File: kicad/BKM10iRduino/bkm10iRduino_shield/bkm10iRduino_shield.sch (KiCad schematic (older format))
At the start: 6 parts, among them J1 RJ45, SW1 SW_SPST, U1 TSOP343xx, U2 MAX485E

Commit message: updated pcb design
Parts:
- removed Brd1: SSD1306, SSD1306:128x64OLED, symbol SSD1306-128x64_OLED:SSD1306
- removed J1: RJ45, Connector_RJ:RJ45_Amphenol_54602-x08_Horizontal, symbol Connector:RJ45
- added C1: C_Small, Capacitor_SMD:CP_Elec_3x5.3, symbol Device:C_Small
- added D3, D4: D_Small_ALT, Diode_SMD:D_1206_3216Metric_Pad1.42x1.75mm_HandSolder, symbol Device:D_Small_ALT
- added D5: SH1106, Connector_PinHeader_2.54mm:PinHeader_1x07_P2.54mm_Vertical, symbol bkm10:SH1106
- added J1: DB9_Male, Connector_Dsub:DSUB-9_Male_Horizontal_P2.77x2.84mm_EdgePinOffset4.94mm_Housed_MountingHolesOffset7.48mm, symbol Connector:DB9_Male
- added R1: R, Resistor_SMD:R_1206_3216Metric_Pad1.30x1.75mm_HandSolder, symbol Device:R
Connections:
- net GND: now also C1.2, D5.7 (GND), J1.1, J1.4, J1.6, J1.9
- net VCC: now also C1.1, D5.6 (VCC), J1.5
- net RES: now reaches A1.11 (D8)
- net RES: now also D5.3 (RES)
- net CS: now reaches A1.12 (D9)
- net CS: now also D5.1 (CS)
- net DC: now reaches A1.13 (D10)
- net DC: now also D5.2 (DC)
- net MOSI: now reaches A1.14 (MOSI)
- net MOSI: now also D5.4 (MOSI)
- net SCK: now reaches A1.16 (SCK)
- net SCK: now also D5.5 (CLK)
- net RS485_RX: now reaches A1.2 (RX1)
- net RS485_RX: now also U2.1 (RO)
- net RS485_RX_ENABLE: now reaches A1.6 (D3)
- net RS485_RX_ENABLE: now also U2.2 (~RE)
- net AB+: now reaches U2.6 (A)
- net AB+: now also D3.1 (K), J1.2, R1.1
- net AB-: now reaches U2.7 (B)
- net AB-: now also D4.1 (K), J1.7, R1.2
- net ~LEARN_BUTTON_IN renamed LEARN_BUTTON_IN
- new net YZ+: D3.2 (A), J1.3
- new net YZ-: D4.2 (A), J1.8
- no-connect marks 25 -> 16

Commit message: pcb redesign
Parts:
- removed D3, D4: D_Small_ALT, Diode_SMD:D_1206_3216Metric_Pad1.42x1.75mm_HandSolder, symbol Device:D_Small_ALT
- removed U2: MAX485E, bkm10rduino:TLL_RS485, symbol Interface_UART:MAX485E
- added C2, C3, C4: C_Small, Capacitor_SMD:C_1812_4532Metric_Pad1.57x3.40mm_HandSolder, symbol Device:C_Small
- added IC1: MAX22508EASA+, SOP50P490X110-10N, symbol SamacSys_Parts:MAX22508EASA+
- C1: footprint Capacitor_SMD:CP_Elec_3x5.3 -> Capacitor_SMD:C_1812_4532Metric_Pad1.57x3.40mm_HandSolder
- J1: footprint Connector_Dsub:DSUB-9_Male_Horizontal_P2.77x2.84mm_EdgePinOffset4.94mm_Housed_MountingHolesOffset7.48mm -> Connector_Dsub:DSUB-9_Male_Vertical_P2.77x2.84mm_MountingHoles
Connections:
- net AB+: now also J1.7, IC1.8 (A); no longer J1.2, R1.1
- net AB-: now also J1.2, IC1.9 (B); no longer J1.7, R1.2
- net GND: now also C2.2, C3.1, C4.1, IC1.5 (GND)
- net RS485_RX: now also IC1.1 (RO)
- net RS485_RX_ENABLE: now also A1.5 (D2), IC1.2 (RE); no longer A1.6 (D3)
- net RS485_TX: now also IC1.4 (DI)
- net RS485_TX_ENABLE: now also A1.6 (D3), IC1.3 (DE); no longer A1.5 (D2)
- net VCC: now also C2.1, C3.2, C4.2, IC1.10 (VCC)
- net YZ+: now also R1.1, IC1.6 (Y)
- net YZ-: now also R1.2, IC1.7 (Z)
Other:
- moved on the sheet: A1, C1, D5, R1, SW1, U1

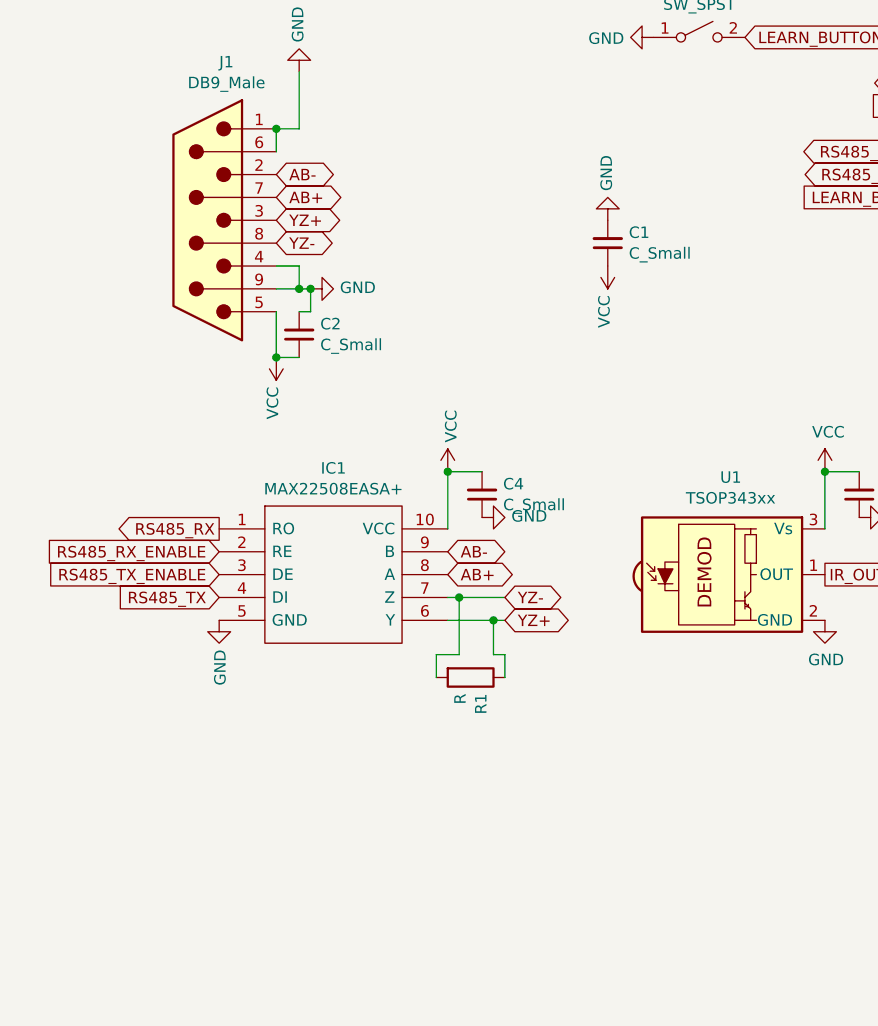
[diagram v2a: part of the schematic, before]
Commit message: many fixes to pcb layout, use full duplex RS485
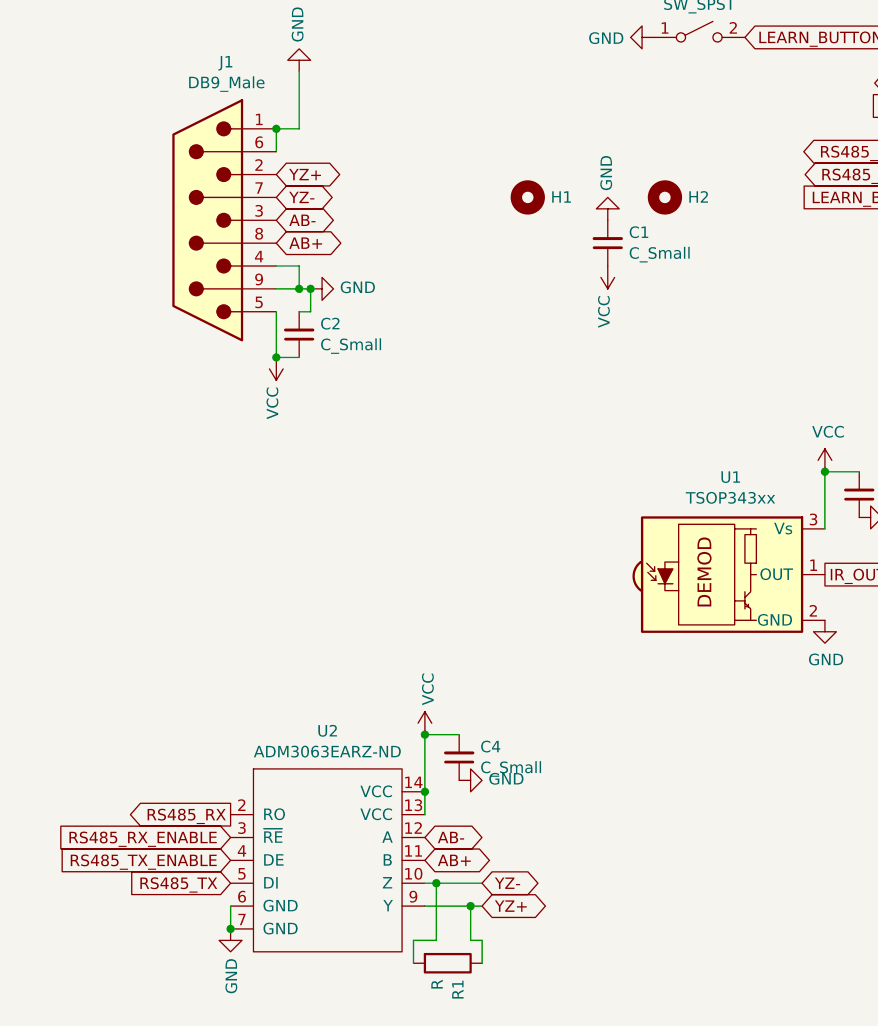
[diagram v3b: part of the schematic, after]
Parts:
- removed IC1: MAX22508EASA+, SOP50P490X110-10N, symbol SamacSys_Parts:MAX22508EASA+
- added H1, H2: MountingHole, MountingHole:MountingHole_3.2mm_M3, symbol Mechanical:MountingHole
- added U2: ADM3063EARZ-ND, Package_SO:SOIC-14_3.9x8.7mm_P1.27mm, symbol bkm10:ADM3063EARZ-ND
- C1, C2, C3, C4: footprint Capacitor_SMD:C_1812_4532Metric_Pad1.57x3.40mm_HandSolder -> Capacitor_SMD:C_1206_3216Metric_Pad1.33x1.80mm_HandSolder
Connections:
- net AB+: now also J1.8, U2.11 (B); no longer J1.7
- net AB-: now also J1.3, U2.12 (A); no longer J1.2
- net GND: now also U2.6 (GND), U2.7 (GND)
- net RS485_RX: now also U2.2 (RO)
- net RS485_RX_ENABLE: now also U2.3 (~RE)
- net RS485_TX: now also U2.5 (DI)
- net RS485_TX_ENABLE: now also U2.4 (DE)
- net VCC: now also U2.13 (VCC), U2.14 (VCC)
- net YZ+: now also J1.2, U2.9 (Y); no longer J1.3
- net YZ-: now also J1.7, U2.10 (Z); no longer J1.8
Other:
- moved on the sheet: C4, R1
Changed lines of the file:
@@
 Text GLabel 6850 2550 0    50   Input ~ 0
 IR_OUT
-Text GLabel 3550 4000 0    50   Input ~ 0
+Text GLabel 3600 5250 0    50   Input ~ 0
 RS485_TX
 Text GLabel 6850 1750 0    50   Output ~ 0
 RS485_TX
-Text GLabel 3550 3900 0    50   Input ~ 0
+Text GLabel 3600 5150 0    50   Input ~ 0
 RS485_TX_ENABLE
 Text GLabel 6850 2150 0    50   Output ~ 0
@@
 Text GLabel 6850 2250 0    50   Input ~ 0
 LEARN_BUTTON_IN
-Text GLabel 3550 3800 0    50   Input ~ 0
+Text GLabel 3600 5050 0    50   Input ~ 0
 RS485_RX_ENABLE
 Text GLabel 6850 2050 0    50   Output ~ 0
 RS485_RX_ENABLE
-Text GLabel 3550 3700 0    50   Output ~ 0
+Text GLabel 3600 4950 0    50   Output ~ 0
 RS485_RX
 Text GLabel 6850 1850 0    50   Input ~ 0
@@
 F 0 "C1" H 5158 2404 50  0000 R CNN
 F 1 "C_Small" H 5158 2495 50  0000 R CNN
-F 2 "Capacitor_SMD:C_1812_4532Metric_Pad1.57x3.40mm_HandSolder" H 5250 2450 50  0001 C CNN
+F 2 "Capacitor_SMD:C_1206_3216Metric_Pad1.33x1.80mm_HandSolder" H 5250 2450 50  0001 C CNN
 F 3 "~" H 5250 2450 50  0001 C CNN
 	1    5250 2450
@@
 L Device:R R1
 U 1 1 618A676D
-P 4650 4350
-F 0 "R1" H 4720 4396 50  0000 L CNN
-F 1 "R" H 4720 4305 50  0000 L CNN
-F 2 "Resistor_SMD:R_1206_3216Metric_Pad1.30x1.75mm_HandSolder" V 4580 4350 50  0001 C CNN
-F 3 "~" H 4650 4350 50  0001 C CNN
-	1    4650 4350
+P 4550 5600
+F 0 "R1" H 4620 5646 50  0000 L CNN
+F 1 "R" H 4620 5555 50  0000 L CNN
+F 2 "Resistor_SMD:R_1206_3216Metric_Pad1.30x1.75mm_HandSolder" V 4480 5600 50  0001 C CNN
+F 3 "~" H 4550 5600 50  0001 C CNN
+	1    4550 5600
 	0    1    1    0
 $EndComp
@@
 	-1   0    0    1
 $EndComp
-Text GLabel 4550 3900 2    50   BiDi ~ 0
+Text GLabel 4450 5150 2    50   BiDi ~ 0
 AB+
-Text GLabel 4550 3800 2    50   BiDi ~ 0
+Text GLabel 4450 5050 2    50   BiDi ~ 0
 AB-
-Text GLabel 3800 2250 2    50   BiDi ~ 0
+Text GLabel 3800 2450 2    50   BiDi ~ 0
 AB+
-Text GLabel 3800 2150 2    50   BiDi ~ 0
+Text GLabel 3800 2350 2    50   BiDi ~ 0
 AB-
 Wire Wire Line
@@
 Wire Wire Line
 	3900 2650 3950 2650
-Text GLabel 4800 4100 2    50   BiDi ~ 0
+Text GLabel 4700 5350 2    50   BiDi ~ 0
 YZ+
-Text GLabel 4800 4000 2    50   BiDi ~ 0
+Text GLabel 4700 5250 2    50   BiDi ~ 0
 YZ-
-Text GLabel 3800 2350 2    50   BiDi ~ 0
+Text GLabel 3800 2150 2    50   BiDi ~ 0
 YZ+
-Text GLabel 3800 2450 2    50   BiDi ~ 0
+Text GLabel 3800 2250 2    50   BiDi ~ 0
 YZ-
 $Comp
 L power:VCC #PWR01
 U 1 1 618B7465
-P 4550 3450
-F 0 "#PWR01" H 4550 3300 50  0001 C CNN
-F 1 "VCC" V 4565 3578 50  0000 L CNN
-F 2 "" H 4550 3450 50  0001 C CNN
-F 3 "" H 4550 3450 50  0001 C CNN
-	1    4550 3450
+P 4450 4600
+F 0 "#PWR01" H 4450 4450 50  0001 C CNN
+F 1 "VCC" V 4465 4728 50  0000 L CNN
+F 2 "" H 4450 4600 50  0001 C CNN
+F 3 "" H 4450 4600 50  0001 C CNN
+	1    4450 4600
 	1    0    0    -1
 $EndComp
@@
 L Device:C_Small C4
 U 1 1 618B84EF
-P 4700 3550
-F 0 "C4" H 4608 3504 50  0000 R CNN
-F 1 "C_Small" H 4608 3595 50  0000 R CNN
-F 2 "Capacitor_SMD:C_1812_4532Metric_Pad1.57x3.40mm_HandSolder" H 4700 3550 50  0001 C CNN
-F 3 "~" H 4700 3550 50  0001 C CNN
-	1    4700 3550
+P 4600 4700
+F 0 "C4" H 4508 4654 50  0000 R CNN
+F 1 "C_Small" H 4508 4745 50  0000 R CNN
+F 2 "Capacitor_SMD:C_1206_3216Metric_Pad1.33x1.80mm_HandSolder" H 4600 4700 50  0001 C CNN
+F 3 "~" H 4600 4700 50  0001 C CNN
+	1    4600 4700
 	-1   0    0    1
 $EndComp
@@
 L power:GND #PWR02
 U 1 1 618B914E
-P 3550 4100
-F 0 "#PWR02" H 3550 3850 50  0001 C CNN
-F 1 "GND" V 3555 3972 50  0000 R CNN
-F 2 "" H 3550 4100 50  0001 C CNN
-F 3 "" H 3550 4100 50  0001 C CNN
-	1    3550 4100
+P 3600 5450
+F 0 "#PWR02" H 3600 5200 50  0001 C CNN
+F 1 "GND" V 3605 5322 50  0000 R CNN
+F 2 "" H 3600 5450 50  0001 C CNN
+F 3 "" H 3600 5450 50  0001 C CNN
+	1    3600 5450
 	1    0    0    -1
 $EndComp
@@
 F 0 "C2" H 3808 2804 50  0000 R CNN
 F 1 "C_Small" H 3808 2895 50  0000 R CNN
-F 2 "Capacitor_SMD:C_1812_4532Metric_Pad1.57x3.40mm_HandSolder" H 3900 2850 50  0001 C CNN
+F 2 "Capacitor_SMD:C_1206_3216Metric_Pad1.33x1.80mm_HandSolder" H 3900 2850 50  0001 C CNN
 F 3 "~" H 3900 2850 50  0001 C CNN
 	1    3900 2850
@@
 F 0 "C3" H 6258 3504 50  0000 R CNN
 F 1 "C_Small" H 6258 3595 50  0000 R CNN
-F 2 "Capacitor_SMD:C_1812_4532Metric_Pad1.57x3.40mm_HandSolder" H 6350 3550 50  0001 C CNN
+F 2 "Capacitor_SMD:C_1206_3216Metric_Pad1.33x1.80mm_HandSolder" H 6350 3550 50  0001 C CNN
 F 3 "~" H 6350 3550 50  0001 C CNN
 	1    6350 3550
@@
 Connection ~ 3950 2650
 Wire Wire Line
-	4550 3450 4550 3700
-Wire Wire Line
-	4550 3450 4700 3450
-Connection ~ 4550 3450
+	4450 4600 4450 4850
+Wire Wire Line
+	4450 4600 4600 4600
+Connection ~ 4450 4600
 $Comp
 L power:GND #PWR03
 U 1 1 618B7AD9
-P 4700 3650
-F 0 "#PWR03" H 4700 3400 50  0001 C CNN
-F 1 "GND" V 4705 3522 50  0000 R CNN
-F 2 "" H 4700 3650 50  0001 C CNN
-F 3 "" H 4700 3650 50  0001 C CNN
-	1    4700 3650
+P 4600 4800
+F 0 "#PWR03" H 4600 4550 50  0001 C CNN
+F 1 "GND" V 4605 4672 50  0000 R CNN
+F 2 "" H 4600 4800 50  0001 C CNN
+F 3 "" H 4600 4800 50  0001 C CNN
+	1    4600 4800
 	0    -1   -1   0
 $EndComp
@@
 	6200 3450 6200 3700
 Connection ~ 6200 3450
-$Comp
-L SamacSys_Parts:MAX22508EASA+ IC1
-U 1 1 618B1646
-P 3550 3700
-F 0 "IC1" H 4050 3965 50  0000 C CNN
-F 1 "MAX22508EASA+" H 4050 3874 50  0000 C CNN
-F 2 "SOP50P490X110-10N" H 4400 3800 50  0001 L CNN
-F 3 "" H 4400 3700 50  0001 L CNN
-F 4 "RS-422/RS-485 Interface IC" H 4400 3600 50  0001 L CNN "Description"
-F 5 "1.1" H 4400 3500 50  0001 L CNN "Height"
-F 6 "" H 4400 3400 50  0001 L CNN "Mouser Part Number"
-F 7 "" H 4400 3300 50  0001 L CNN "Mouser Price/Stock"
-F 8 "Maxim Integrated" H 4400 3200 50  0001 L CNN "Manufacturer_Name"
-F 9 "MAX22508EASA+" H 4400 3100 50  0001 L CNN "Manufacturer_Part_Number"
-	1    3550 3700
-	1    0    0    -1
-$EndComp
-Wire Wire Line
-	4800 4000 4600 4000
-Wire Wire Line
-	4800 4100 4750 4100
-Wire Wire Line
-	4800 4350 4800 4250
-Wire Wire Line
-	4800 4250 4750 4250
-Wire Wire Line
-	4750 4250 4750 4100
-Connection ~ 4750 4100
-Wire Wire Line
-	4750 4100 4550 4100
-Wire Wire Line
-	4500 4350 4500 4250
-Wire Wire Line
-	4500 4250 4600 4250
-Wire Wire Line
-	4600 4250 4600 4000
-Connection ~ 4600 4000
-Wire Wire Line
-	4600 4000 4550 4000
+Wire Wire Line
+	4700 5250 4500 5250
+Wire Wire Line
+	4700 5350 4650 5350
+Wire Wire Line
+	4700 5600 4700 5500
+Wire Wire Line
+	4700 5500 4650 5500
+Wire Wire Line
+	4650 5500 4650 5350
+Connection ~ 4650 5350
+Wire Wire Line
+	4650 5350 4450 5350
+Wire Wire Line
+	4400 5600 4400 5500
+Wire Wire Line
+	4400 5500 4500 5500
+Wire Wire Line
+	4500 5500 4500 5250
+Connection ~ 4500 5250
+Wire Wire Line
+	4500 5250 4450 5250
+$Comp
+L bkm10:ADM3063EARZ-ND U2
+U 1 1 619EE6CE
+P 4000 4600
+F 0 "U2" H 4025 4615 50  0000 C CNN
+F 1 "ADM3063EARZ-ND" H 4025 4524 50  0000 C CNN
+F 2 "Package_SO:SOIC-14_3.9x8.7mm_P1.27mm" H 4000 4600 50  0001 C CNN
+F 3 "https://www.analog.com/media/en/technical-documentation/data-sheets/ADM3061E-3062E-3063E-3064E-3065E-3066E-3067E-3068E.pdf" H 4000 4600 50  0001 C CNN
+	1    4000 4600
+	1    0    0    -1
+$EndComp
+Wire Wire Line
+	4450 4850 4450 4950
+Connection ~ 4450 4850
+Wire Wire Line
+	3600 5350 3600 5450
+Connection ~ 3600 5450
+$Comp
+L Mechanical:MountingHole H1
+U 1 1 61A0BC8D
+P 4900 2250
+F 0 "H1" H 5000 2250 50  0000 L CNN
+F 1 "MountingHole" H 5000 2208 50  0001 L CNN
+F 2 "MountingHole:MountingHole_3.2mm_M3" H 4900 2250 50  0001 C CNN
+F 3 "~" H 4900 2250 50  0001 C CNN
+	1    4900 2250
+	1    0    0    -1
+$EndComp
+$Comp
+L Mechanical:MountingHole H2
+U 1 1 61A0E14E
+P 5500 2250
+F 0 "H2" H 5600 2250 50  0000 L CNN
+F 1 "MountingHole" H 5600 2208 50  0001 L CNN
+F 2 "MountingHole:MountingHole_3.2mm_M3" H 5500 2250 50  0001 C CNN
+F 3 "~" H 5500 2250 50  0001 C CNN
+	1    5500 2250
+	1    0    0    -1
+$EndComp
 $EndSCHEMATC

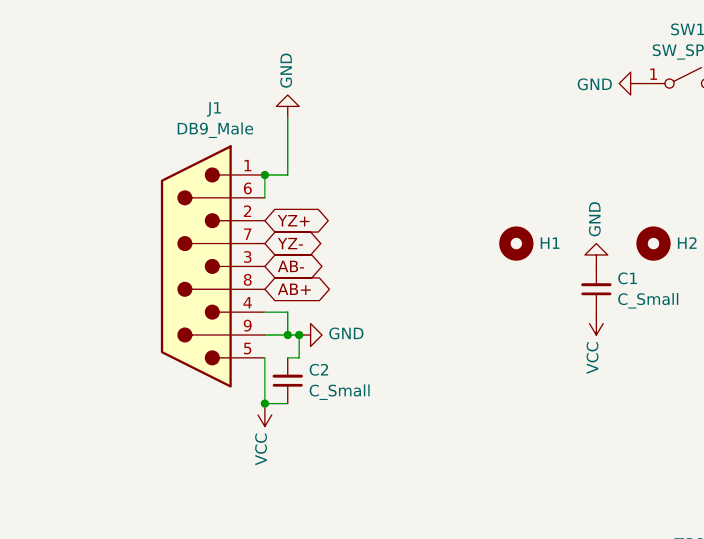
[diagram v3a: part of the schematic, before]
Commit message: add 2 layer PBC and also a RP2040 version
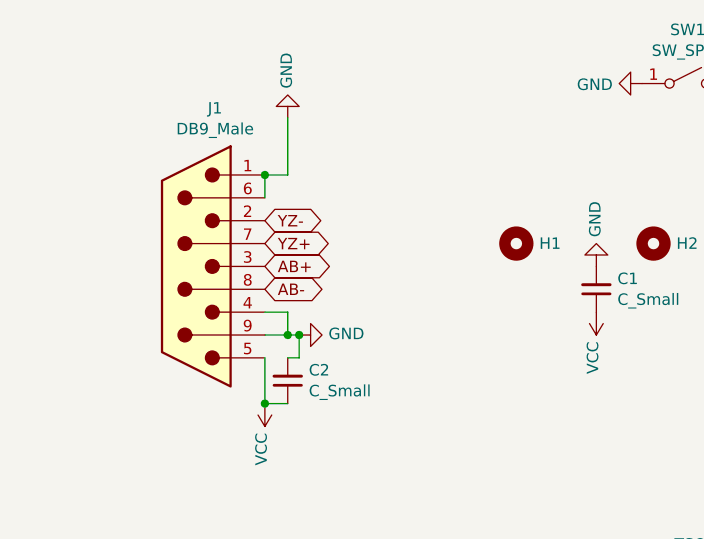
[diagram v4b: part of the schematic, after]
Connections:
- net AB+: now also J1.3; no longer J1.8
- net AB-: now also J1.8; no longer J1.3
- net YZ+: now also J1.7; no longer J1.2
- net YZ-: now also J1.2; no longer J1.7
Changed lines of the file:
@@
 AB-
 Text GLabel 3800 2450 2    50   BiDi ~ 0
+AB-
+Text GLabel 3800 2350 2    50   BiDi ~ 0
 AB+
-Text GLabel 3800 2350 2    50   BiDi ~ 0
-AB-
 Wire Wire Line
 	3800 2650 3900 2650
@@
 YZ-
 Text GLabel 3800 2150 2    50   BiDi ~ 0
+YZ-
+Text GLabel 3800 2250 2    50   BiDi ~ 0
 YZ+
-Text GLabel 3800 2250 2    50   BiDi ~ 0
-YZ-
 $Comp
 L power:VCC #PWR01
